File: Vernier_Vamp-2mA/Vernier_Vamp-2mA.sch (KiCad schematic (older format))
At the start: 6 parts, among them J1 Conn_01x02, J2 RJ45, J3 Screw_Terminal_01x04, J5 Conn_Coaxial, J6 Conn_Coaxial, J7 Conn_Coaxial

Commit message: 1.0B fixes for 2mA (schematic)
Added 1.0B fixes to the 2mA version related to schematic cleanup, and addition of hysteresis and alternative way to power nano.
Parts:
- J5: value Conn_Coaxial -> Channel 3
- J6: value Conn_Coaxial -> Channel 2
- J7: value Conn_Coaxial -> Channel 1
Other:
- note added: "BNC coil driver output\n"
- note added: "Enclosure: Hammond 1455N1601BK\n160 X 103 X 53\n\nAnodised aluminium"
- note added: "RJ45 coil driver output\n"
- note removed: "BNC coil driver output\n(Requested by Harry)"
- note removed: "Enclosure: Hammond 1455N1601BK\n160 X 103 X 53\n\nAnodised aluminum"
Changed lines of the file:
@@
 $Descr A4 11693 8268
 encoding utf-8
-Sheet 1 5
-Title "\"Vernier Vamp\" Coil Driver - 200mA"
-Date "2020-02-04"
-Rev "1.0A"
+Sheet 1 7
+Title "\"Vernier Vamp\" Coil Driver - 2mA"
+Date "2020-05-05"
+Rev "1.0B"
 Comp "Strathclyde University"
 Comment1 "Designed by: Marcin Mrozowski"
@@
 P 9600 1650
 F 0 "J5" H 9700 1625 50  0000 L CNN
-F 1 "Conn_Coaxial" H 9700 1534 50  0000 L CNN
+F 1 "Channel 3" H 9700 1534 50  0000 L CNN
 F 2 "Connector_Coaxial:BNC_Amphenol_031-6575_Horizontal" H 9600 1650 50  0001 C CNN
 F 3 " ~" H 9600 1650 50  0001 C CNN
@@
 P 9600 2100
 F 0 "J6" H 9700 2075 50  0000 L CNN
-F 1 "Conn_Coaxial" H 9700 1984 50  0000 L CNN
+F 1 "Channel 2" H 9700 1984 50  0000 L CNN
 F 2 "Connector_Coaxial:BNC_Amphenol_031-6575_Horizontal" H 9600 2100 50  0001 C CNN
 F 3 " ~" H 9600 2100 50  0001 C CNN
@@
 P 9600 2500
 F 0 "J7" H 9700 2475 50  0000 L CNN
-F 1 "Conn_Coaxial" H 9700 2384 50  0000 L CNN
+F 1 "Channel 1" H 9700 2384 50  0000 L CNN
 F 2 "Connector_Coaxial:BNC_Amphenol_031-6575_Horizontal" H 9600 2500 50  0001 C CNN
 F 3 " ~" H 9600 2500 50  0001 C CNN
@@
 	8400 3600 8000 3600
 Text Notes 9250 1500 0    50   ~ 0
-BNC coil driver output\n(Requested by Harry)
+BNC coil driver output\n
 Text Notes 10150 3400 0    50   ~ 0
 Unshielded RJ45\nChannel 3 (1 2)\nChannel 2 (4 5)\nChannel 1 (7 8)
@@
 Screw terminal for power\nTied to binding posts at the back
 Text Notes 4900 6500 0    118  ~ 0
-Enclosure: Hammond 1455N1601BK\n160 X 103 X 53\n\nAnodised aluminum
+Enclosure: Hammond 1455N1601BK\n160 X 103 X 53\n\nAnodised aluminium
+Text Notes 9250 3800 0    50   ~ 0
+RJ45 coil driver output\n
+$Sheet
+S 1050 6800 750  700
+U 5EB165A9
+F0 "Mounting_Holes" 50
+F1 "Mounting_Holes.sch" 50
+$EndSheet
 $EndSCHEMATC

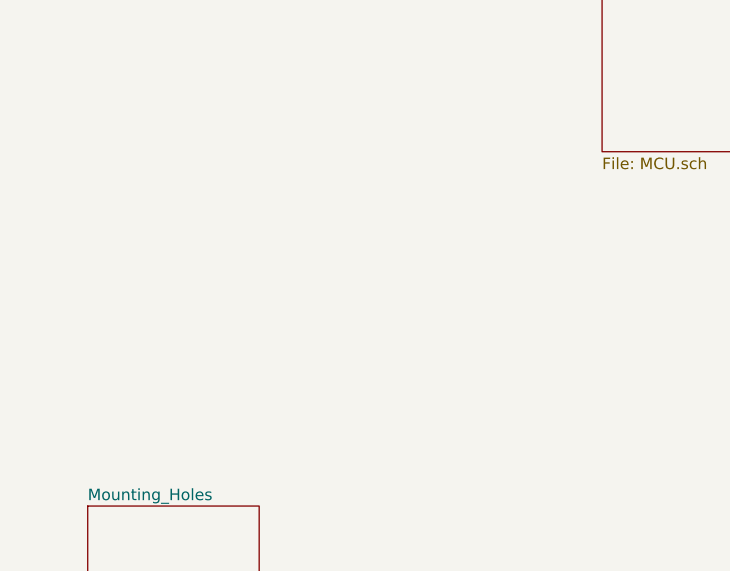
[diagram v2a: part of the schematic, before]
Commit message: Issue fixes
This commit, addresses following issues:
-Stray current at the output with only USB plugged in
-RFI Shield over analogue circuitry
-Wrong BNC connector footprint

Some general layout optimisation
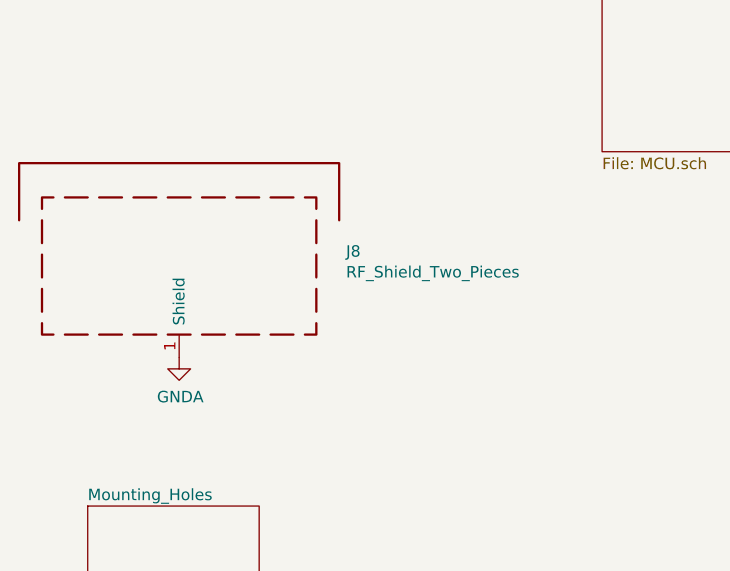
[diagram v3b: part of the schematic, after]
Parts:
- added J8: RF_Shield_Two_Pieces, MS548-10F:MS548-10C, symbol Device:RF_Shield_Two_Pieces
- J1: footprint Connector_PinHeader_1.27mm:PinHeader_1x02_P1.27mm_Vertical -> Connector_PinSocket_1.00mm:PinSocket_1x02_P1.00mm_Vertical
- J5, J6, J7: footprint Connector_Coaxial:BNC_Amphenol_031-6575_Horizontal -> Connector_Coaxial:BNC_Amphenol_B6252HB-NPP3G-50_Horizontal
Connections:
- net GNDA: now also J8.1 (Shield)
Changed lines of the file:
@@
 F 0 "J1" H 8780 4192 50  0000 L CNN
 F 1 "Conn_01x02" H 8780 4101 50  0000 L CNN
-F 2 "Connector_PinHeader_1.27mm:PinHeader_1x02_P1.27mm_Vertical" H 8700 4200 50  0001 C CNN
+F 2 "Connector_PinSocket_1.00mm:PinSocket_1x02_P1.00mm_Vertical" H 8700 4200 50  0001 C CNN
 F 3 "~" H 8700 4200 50  0001 C CNN
 	1    8700 4200
@@
 F 0 "J5" H 9700 1625 50  0000 L CNN
 F 1 "Channel 3" H 9700 1534 50  0000 L CNN
-F 2 "Connector_Coaxial:BNC_Amphenol_031-6575_Horizontal" H 9600 1650 50  0001 C CNN
+F 2 "Connector_Coaxial:BNC_Amphenol_B6252HB-NPP3G-50_Horizontal" H 9600 1650 50  0001 C CNN
 F 3 " ~" H 9600 1650 50  0001 C CNN
 	1    9600 1650
@@
 F 0 "J6" H 9700 2075 50  0000 L CNN
 F 1 "Channel 2" H 9700 1984 50  0000 L CNN
-F 2 "Connector_Coaxial:BNC_Amphenol_031-6575_Horizontal" H 9600 2100 50  0001 C CNN
+F 2 "Connector_Coaxial:BNC_Amphenol_B6252HB-NPP3G-50_Horizontal" H 9600 2100 50  0001 C CNN
 F 3 " ~" H 9600 2100 50  0001 C CNN
 	1    9600 2100
@@
 F 0 "J7" H 9700 2475 50  0000 L CNN
 F 1 "Channel 1" H 9700 2384 50  0000 L CNN
-F 2 "Connector_Coaxial:BNC_Amphenol_031-6575_Horizontal" H 9600 2500 50  0001 C CNN
+F 2 "Connector_Coaxial:BNC_Amphenol_B6252HB-NPP3G-50_Horizontal" H 9600 2500 50  0001 C CNN
 F 3 " ~" H 9600 2500 50  0001 C CNN
 	1    9600 2500
@@
 F1 "Mounting_Holes.sch" 50
 $EndSheet
+$Comp
+L Device:RF_Shield_Two_Pieces J8
+U 1 1 5FC43AD0
+P 1450 5750
+F 0 "J8" H 2180 5814 50  0000 L CNN
+F 1 "RF_Shield_Two_Pieces" H 2180 5723 50  0000 L CNN
+F 2 "MS548-10F:MS548-10C" H 1450 5650 50  0001 C CNN
+F 3 "~" H 1450 5650 50  0001 C CNN
+	1    1450 5750
+	1    0    0    -1
+$EndComp
+$Comp
+L power:GNDA #PWR?
+U 1 1 5FC46947
+P 1450 6150
+AR Path="/5E1DD476/5FC46947" Ref="#PWR?"  Part="1"
+AR Path="/5FC46947" Ref="#PWR0213"  Part="1"
+F 0 "#PWR0213" H 1450 5900 50  0001 C CNN
+F 1 "GNDA" H 1455 5977 50  0000 C CNN
+F 2 "" H 1450 6150 50  0001 C CNN
+F 3 "" H 1450 6150 50  0001 C CNN
+	1    1450 6150
+	1    0    0    -1
+$EndComp
 $EndSCHEMATC

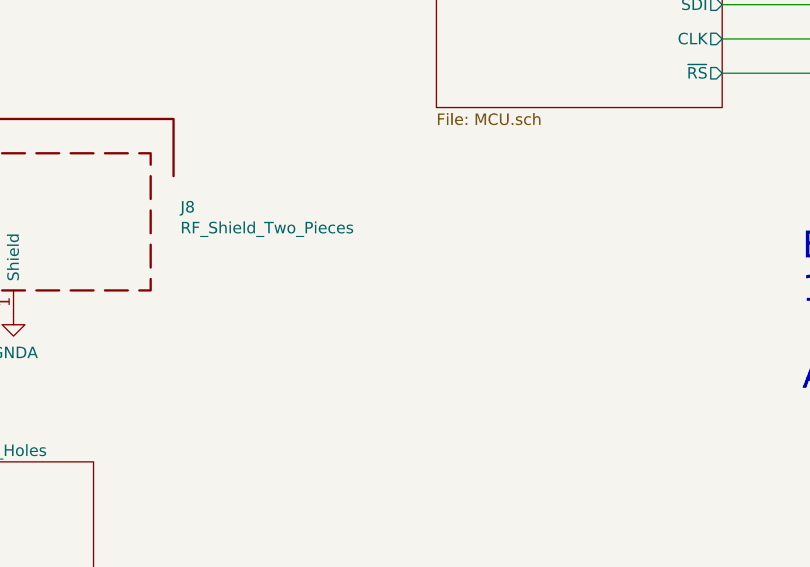
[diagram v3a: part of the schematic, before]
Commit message: Silkscreen fixes
Silkscreen settings changed so that references are not obstructed by the shield.
-Added magnetic field direction designation for each channel.
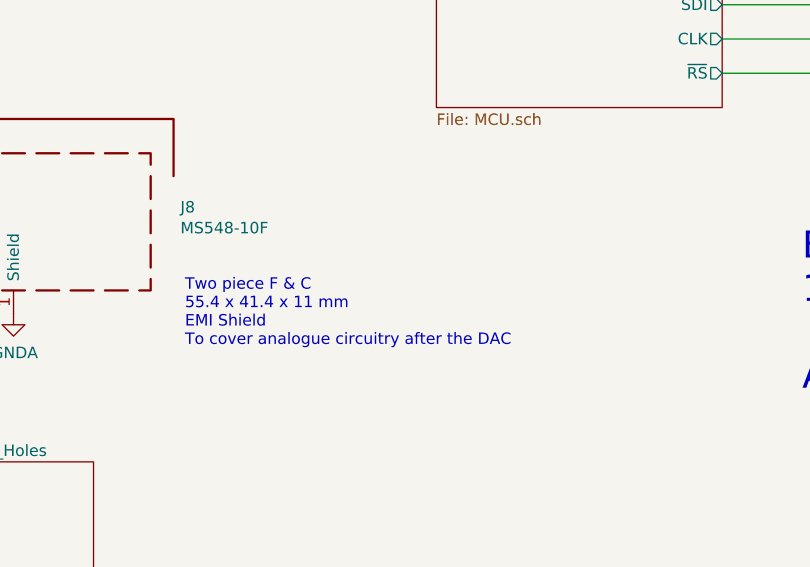
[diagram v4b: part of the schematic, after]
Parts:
- J8: value RF_Shield_Two_Pieces -> MS548-10F
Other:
- note added: "Two piece F & C\n55.4 x 41.4 x 11 mm\nEMI Shield\nTo cover analogue circuitry after the DAC"
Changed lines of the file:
@@
 P 1450 5750
 F 0 "J8" H 2180 5814 50  0000 L CNN
-F 1 "RF_Shield_Two_Pieces" H 2180 5723 50  0000 L CNN
+F 1 "MS548-10F" H 2180 5723 50  0000 L CNN
 F 2 "MS548-10F:MS548-10C" H 1450 5650 50  0001 C CNN
 F 3 "~" H 1450 5650 50  0001 C CNN
@@
 	1    0    0    -1
 $EndComp
+Text Notes 2200 6300 0    50   ~ 0
+Two piece F & C\n55.4 x 41.4 x 11 mm\nEMI Shield\nTo cover analogue circuitry after the DAC
 $EndSCHEMATC

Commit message: Change of J1 connector courtyard
PCB footprint change:
-J1 (1 mm pinheader) courtyard had been changed to pass DRC
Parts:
- J1: footprint Connector_PinSocket_1.00mm:PinSocket_1x02_P1.00mm_Vertical -> Dummy_conn_01x02:PinSocket_1x02_P1.00mm_Vertical_CUSTOM_CYD
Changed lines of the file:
@@
 F 0 "J1" H 8780 4192 50  0000 L CNN
 F 1 "Conn_01x02" H 8780 4101 50  0000 L CNN
-F 2 "Connector_PinSocket_1.00mm:PinSocket_1x02_P1.00mm_Vertical" H 8700 4200 50  0001 C CNN
+F 2 "Dummy_conn_01x02:PinSocket_1x02_P1.00mm_Vertical_CUSTOM_CYD" H 8700 4200 50  0001 C CNN
 F 3 "~" H 8700 4200 50  0001 C CNN
 	1    8700 4200
